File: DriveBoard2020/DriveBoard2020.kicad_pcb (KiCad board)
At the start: 2 copper layers, 78 parts, among them SW0 SW_SPST, SW1 SW_Push, SW2 SW_Push, SW3 SW_Push, SW4 SW_Push, SW5 SW_Push, SW6 SW_Push, SW7 SW_Push, SW8 SW_Push, SW9 SW_Push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

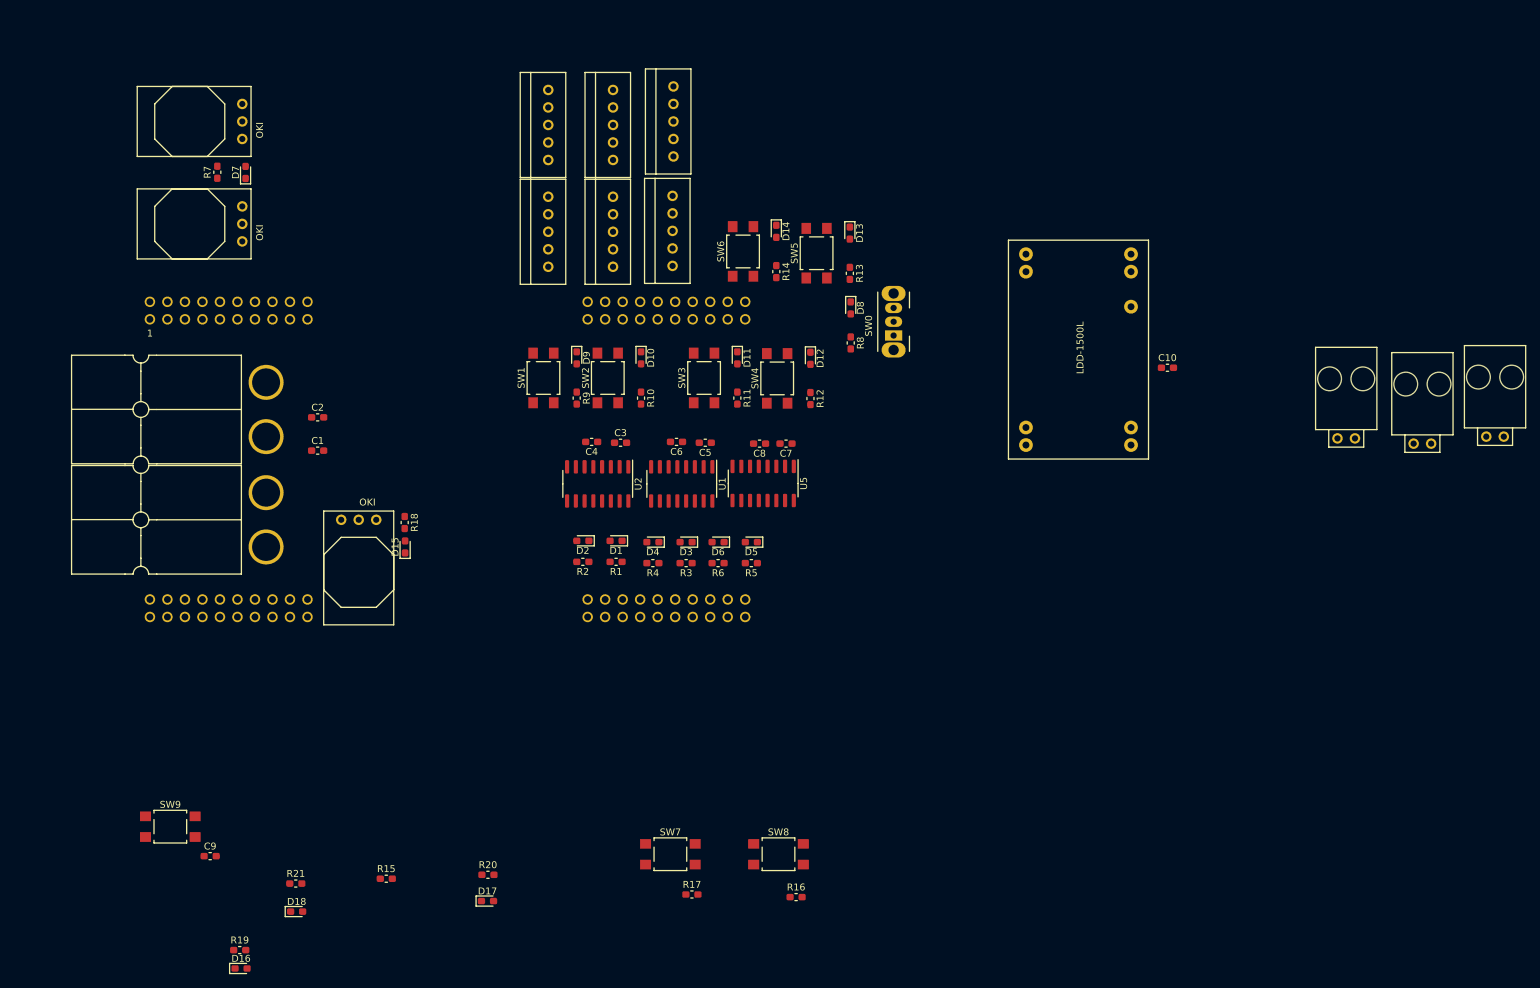
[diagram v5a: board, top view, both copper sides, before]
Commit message: finished placing components on layout
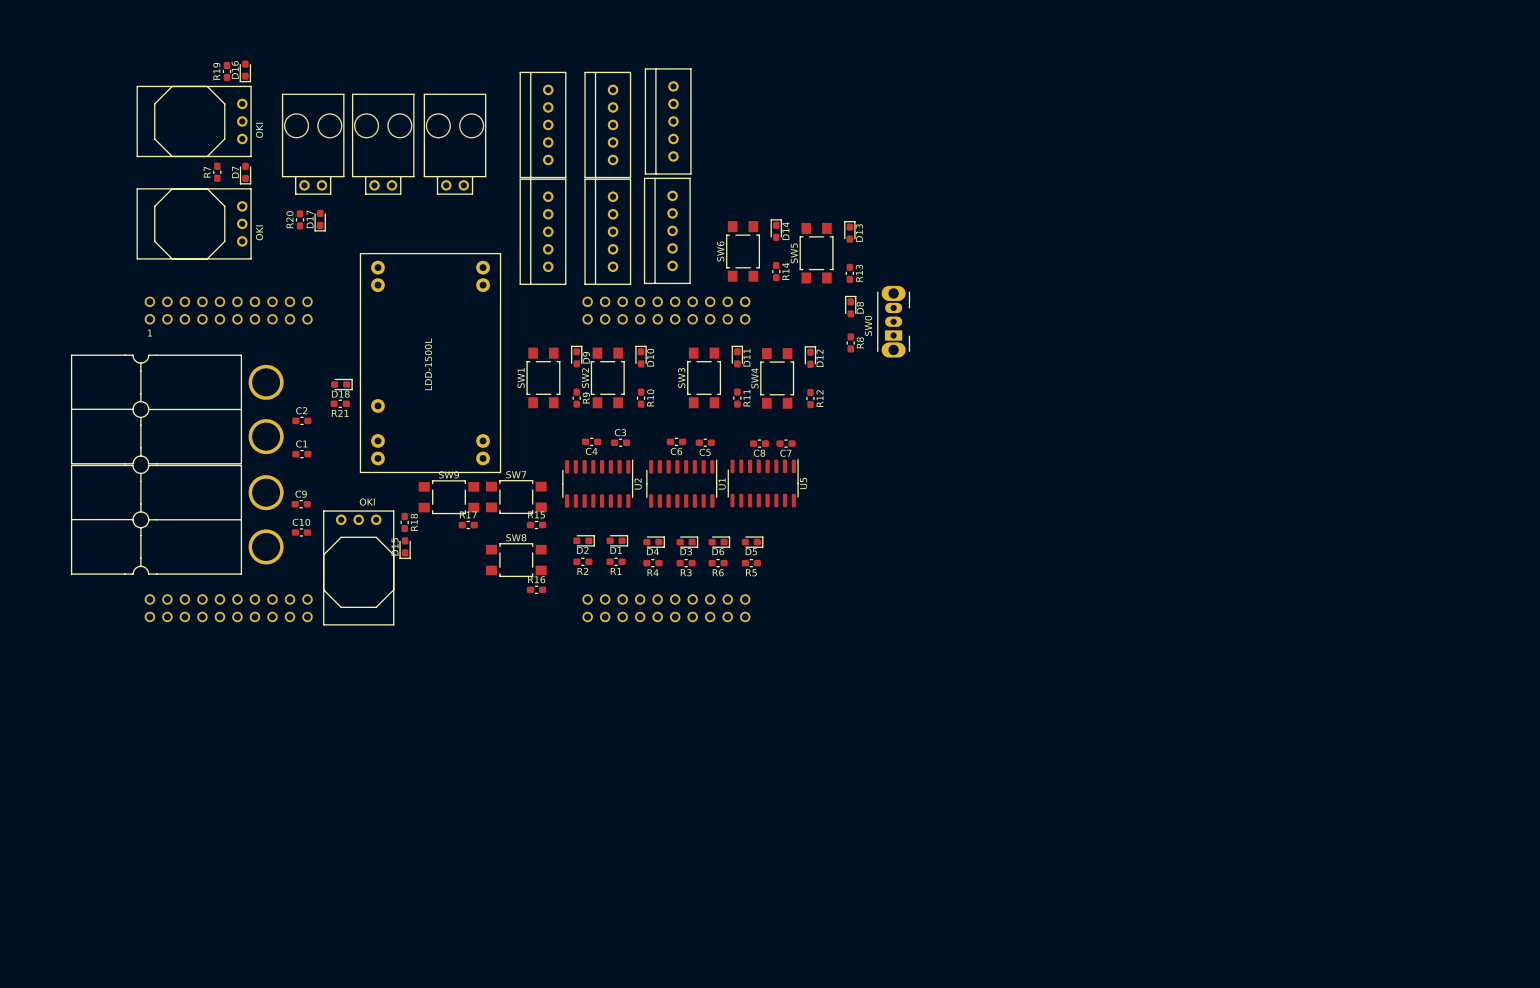
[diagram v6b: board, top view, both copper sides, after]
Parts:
- moved Conn11 155.3 mm to (108.2, 46.5)
- moved Conn10 155.2 mm to (118.6, 46.5)
- moved Conn9 154.3 mm to (98.0, 46.5)
- moved D16 130.3 mm to (88.2, 29.8), turned to 90 degrees
- moved C10 127.9 mm to (96.3, 96.8)
- moved R19 127.5 mm to (85.5, 30.0), turned to 90 degrees
- moved D17 101.8 mm to (99.1, 51.4), turned to 90 degrees
- moved R20 98.8 mm to (96.1, 51.5), turned to 90 degrees
- moved U8 79.5 mm to (125.2, 56.4), turned to 180 degrees
- moved D18 76.7 mm to (102.0, 75.4), turned to 180 degrees
- moved R21 69.9 mm to (102.0, 78.2), turned to 180 degrees
- moved R17 62.7 mm to (120.5, 95.8)
- moved SW9 62.6 mm to (117.7, 91.7)
- moved R16 58.4 mm to (130.4, 105.2)
- moved SW8 57.2 mm to (127.5, 100.8)
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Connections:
- Conn8 pad 2: (no net) -> +12VA
- U4 pad PA7: Headlight_OnOff_PWM -> Net-(U4-PadPA7)
- U4 pad PC7: Net-(U4-PadPC7) -> Headlight_OnOff_PWM
- U4 pad PF1: Dout_NeoPixel -> Net-(U4-PadPF1)
- U4 pad PP2: Net-(U4-PadPP2) -> Dout_NeoPixel

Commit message: traces to layout
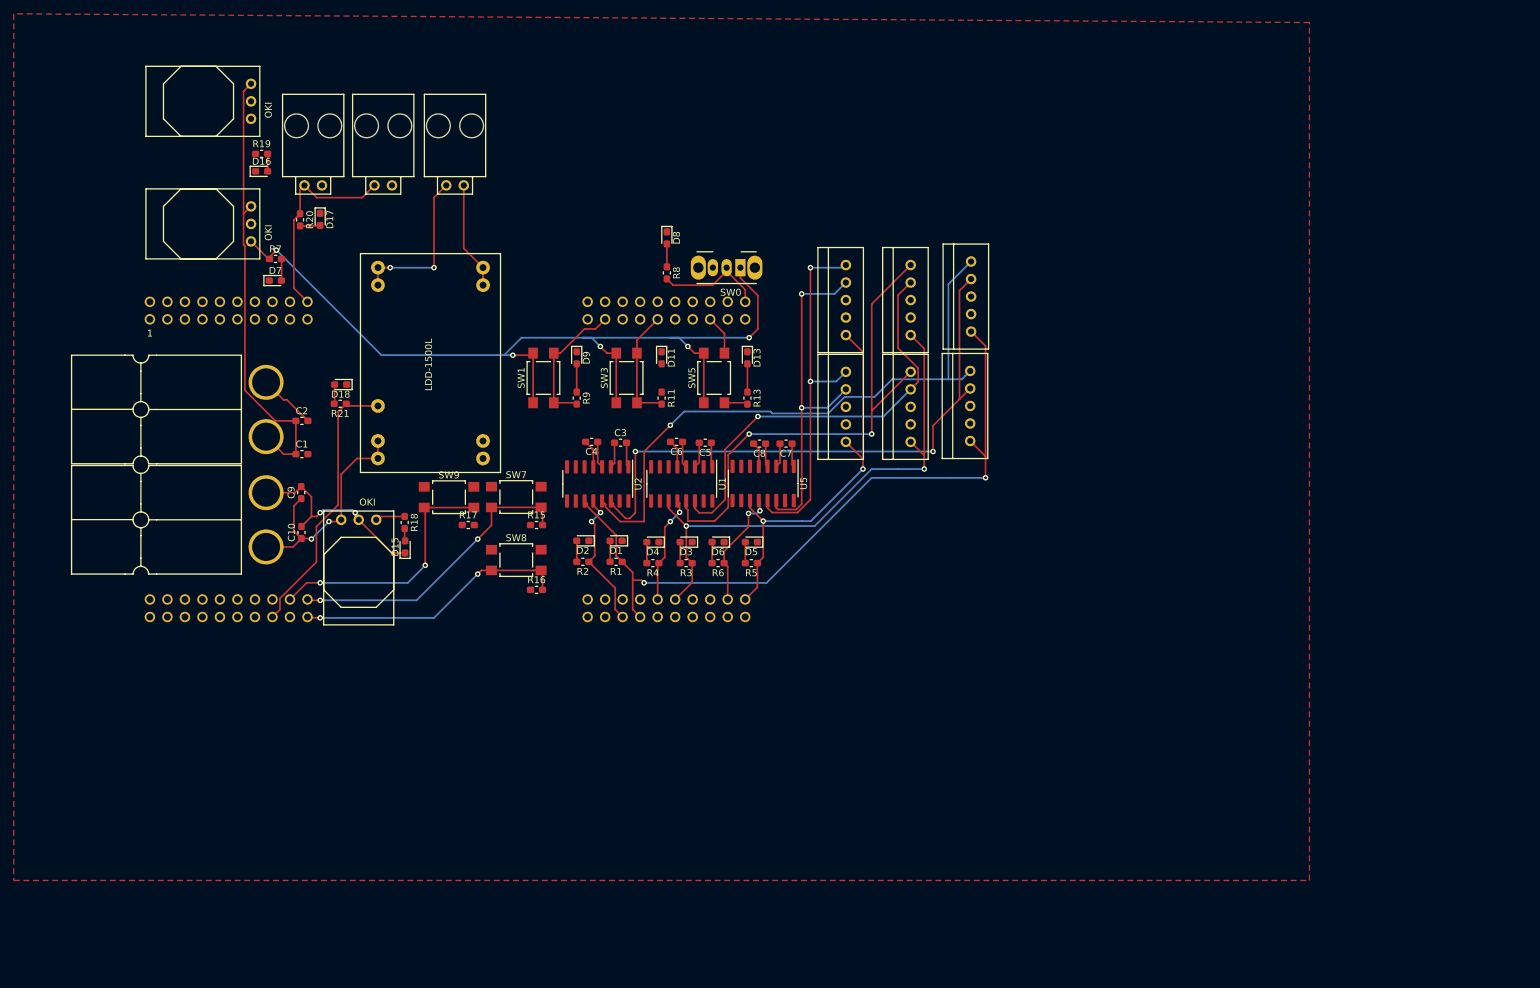
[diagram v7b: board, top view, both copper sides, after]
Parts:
- removed D10, D12, D14: LED, LED_SMD:LED_0603_1608Metric_Pad1.05x0.95mm_HandSolder
- removed R10, R12, R14: 500, Resistor_SMD:R_0603_1608Metric_Pad1.05x0.95mm_HandSolder
- removed SW2, SW4, SW6: SW_Push, Button_Switch_SMD:SW_SPST_TL3305A
- moved Conn2 50.1 mm to (193.5, 62.6)
- moved Conn4 50.1 mm to (175.3, 63.1)
- moved Conn7 50.1 mm to (175.3, 78.6)
- moved Conn3 50.1 mm to (184.7, 63.1)
- moved Conn5 50.1 mm to (193.4, 78.5)
- moved Conn6 50.1 mm to (184.7, 78.6)
- moved D8 28.5 mm to (149.4, 54.1)
- moved R8 28.5 mm to (149.4, 59.2)
- moved SW0 24.3 mm to (160.0, 58.4), turned to 180 degrees
- moved D13 23.4 mm to (161.0, 71.5)
- moved R13 23.4 mm to (161.0, 77.3)
- moved SW5 23.4 mm to (156.2, 74.4)
- moved D7 16.3 mm to (92.6, 60.3), turned to 0 degrees
- moved R7 15.1 mm to (92.6, 57.1), turned to 0 degrees
- moved D16 14.9 mm to (90.6, 44.5), turned to 0 degrees
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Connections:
- R11 pad 2: ML_Motor -> Middle_Motor
- R13 pad 2: RL_Motor -> Rear_Motor
- R19 pad 1: +5VL -> +5V
- R9 pad 2: FL_Motor -> Front_Motor
- SW1 pad 2: FL_Motor -> Front_Motor
- SW3 pad 2: ML_Motor -> Middle_Motor
- SW5 pad 2: RL_Motor -> Rear_Motor
- U4 pad PB3: Net-(U4-PadPB3) -> NeoPixel_White
- U4 pad PH1: ML_Motor -> Rear_Motor
- U4 pad PK4: Net-(U4-PadPK4) -> Front_Motor
- U4 pad PK5: FL_Motor -> Net-(U4-PadPK5)
- U4 pad PK6: MR_Motor -> Net-(U4-PadPK6)
- U4 pad PL4: NeoPixel_White -> Net-(U4-PadPL4)
- U4 pad PL5: NeoPixel_Pattern -> Net-(U4-PadPL5)
- U4 pad PM0: FR_Motor -> Net-(U4-PadPM0)
- U4 pad PM1: Net-(U4-PadPM1) -> Middle_Motor
- U4 pad PM3: Headlight_Power -> Net-(U4-PadPM3)
- U4 pad PM4: Net-(U4-PadPM4) -> NeoPixel_Pattern
- U4 pad PM5: Net-(U4-PadPM5) -> Headlight_Power
- U4 pad PP3: RR_Motor -> Net-(U4-PadPP3)
- U4 pad PQ1: RL_Motor -> Net-(U4-PadPQ1)
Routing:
- net +3V3: track 0.00 -> 130.6 mm, vias 0 -> 5
- net Tx6: track 0.00 -> 103.0 mm, vias 0 -> 2
- net R1_In: track 0.00 -> 88.5 mm, vias 0 -> 1
- net T1_Out: track 0.00 -> 86.7 mm, vias 0 -> 2
- net Tx4: track 0.00 -> 77.7 mm, vias 0 -> 2
- net R2_In: track 0.00 -> 74.2 mm, vias 0 -> 2
- net +12V: track 0.00 -> 66.0 mm
- net T2_Out: track 0.00 -> 62.3 mm, vias 0 -> 1
- net Tx3: track 0.00 -> 57.8 mm, vias 0 -> 2
- net R3_In: track 0.00 -> 53.0 mm, vias 0 -> 3
- net T3_Out: track 0.00 -> 50.3 mm, vias 0 -> 2
- net Headlight_Power: track 0.00 -> 43.7 mm, vias 0 -> 2
- net Headlight_OnOff_PWM: track 0.00 -> 40.1 mm
- net NeoPixel_White: track 0.00 -> 39.7 mm, vias 0 -> 2
- net NeoPixel_Pattern: track 0.00 -> 37.3 mm, vias 0 -> 2
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- added copper zone on F.Cu, net GND

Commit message: edge cuts
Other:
- board outline added: 124.5 x 107.4 mm
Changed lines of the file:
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@@
   (general
     (thickness 1.6)
-    (drawings 0)
+    (drawings 20)
     (tracks 394)
     (zones 0)
@@
     )
   )
+  (gr_line (start 73.152 28.321) (end 197.612 28.321) (layer Edge.Cuts) (width 0.05))
+  (gr_line (start 73.152 54.483) (end 73.152 28.321) (layer Edge.Cuts) (width 0.05))
+  (gr_line (start 73.152 121.031) (end 73.152 54.483) (layer Edge.Cuts) (width 0.05))
+  (gr_arc (start 73.152 123.063) (end 73.152 125.095) (angle -180) (layer Edge.Cuts) (width 0.05))
+  (gr_line (start 73.152 133.731) (end 73.152 125.095) (layer Edge.Cuts) (width 0.05))
+  (gr_arc (start 75.184 133.731) (end 73.152 133.731) (angle -90) (layer Edge.Cuts) (width 0.05))
+  (gr_line (start 124.587 135.763) (end 75.184 135.763) (layer Edge.Cuts) (width 0.05))
+  (gr_line (start 197.612 54.483) (end 197.612 28.321) (layer Edge.Cuts) (width 0.05))
+  (gr_line (start 197.612 88.011) (end 197.612 54.483) (layer Edge.Cuts) (width 0.05))
+  (gr_arc (start 195.58 88.011) (end 195.58 90.043) (angle -90) (layer Edge.Cuts) (width 0.05))
+  (gr_line (start 195.453 90.043) (end 195.58 90.043) (layer Edge.Cuts) (width 0.05))
+  (gr_line (start 179.705 90.043) (end 195.453 90.043) (layer Edge.Cuts) (width 0.05))
+  (gr_line (start 179.705 110.871) (end 179.705 90.043) (layer Edge.Cuts) (width 0.05))
+  (gr_line (start 195.58 110.871) (end 179.705 110.871) (layer Edge.Cuts) (width 0.05))
+  (gr_arc (start 195.58 112.903) (end 197.612 112.903) (angle -90) (layer Edge.Cuts) (width 0.05))
+  (gr_line (start 197.612 121.031) (end 197.612 112.903) (layer Edge.Cuts) (width 0.05))
+  (gr_arc (start 197.612 123.063) (end 197.612 121.031) (angle -180) (layer Edge.Cuts) (width 0.05))
+  (gr_line (start 197.612 133.731) (end 197.612 125.095) (layer Edge.Cuts) (width 0.05))
+  (gr_arc (start 195.58 133.731) (end 195.58 135.763) (angle -90) (layer Edge.Cuts) (width 0.05))
+  (gr_line (start 124.587 135.763) (end 195.58 135.763) (layer Edge.Cuts) (width 0.05))
   (segment (start 96.782928 80.145928) (end 97.282 80.645) (width 0.25) (layer F.Cu) (net 1))
   (segment (start 94.233999 77.596999) (end 96.782928 80.145928) (width 0.25) (layer F.Cu) (net 1))
@@
   (segment (start 191.80175 77.50175) (end 193.3575 75.946) (width 0.25) (layer F.Cu) (net 44))
   (segment (start 187.96 81.3435) (end 191.80175 77.50175) (width 0.25) (layer F.Cu) (net 44))
-  (segment (start 132.945 71.872) (end 132.945 78.022) (width 0.25) (layer F.Cu) (net 133))
-  (segment (start 132.945 70.822) (end 132.945 71.872) (width 0.25) (layer F.Cu) (net 133))
-  (segment (start 136.075 78.022) (end 136.271 78.218) (width 0.25) (layer F.Cu) (net 133))
-  (segment (start 132.945 78.022) (end 136.075 78.022) (width 0.25) (layer F.Cu) (net 133))
-  (segment (start 133.895 70.822) (end 137.407 67.31) (width 0.25) (layer F.Cu) (net 133))
-  (segment (start 132.945 70.822) (end 133.895 70.822) (width 0.25) (layer F.Cu) (net 133))
   (segment (start 95.844428 97.213428) (end 96.3435 97.7125) (width 0.25) (layer F.Cu) (net 69))
   (segment (start 95.25 96.619) (end 95.844428 97.213428) (width 0.25) (layer F.Cu) (net 69))
@@
   (segment (start 101.65799 92.849008) (end 98.515001 95.991997) (width 0.25) (layer F.Cu) (net 83))
   (segment (start 102.842 78.1685) (end 101.65799 79.35251) (width 0.25) (layer F.Cu) (net 83))
+  (segment (start 132.945 71.872) (end 132.945 78.022) (width 0.25) (layer F.Cu) (net 133))
+  (segment (start 132.945 70.822) (end 132.945 71.872) (width 0.25) (layer F.Cu) (net 133))
+  (segment (start 136.075 78.022) (end 136.271 78.218) (width 0.25) (layer F.Cu) (net 133))
+  (segment (start 132.945 78.022) (end 136.075 78.022) (width 0.25) (layer F.Cu) (net 133))
+  (segment (start 133.895 70.822) (end 137.407 67.31) (width 0.25) (layer F.Cu) (net 133))
+  (segment (start 132.945 70.822) (end 133.895 70.822) (width 0.25) (layer F.Cu) (net 133))
   (segment (start 139.0015 67.31) (end 137.407 67.31) (width 0.25) (layer F.Cu) (net 133))
   (segment (start 140.3985 65.913) (end 139.0015 67.31) (width 0.25) (layer F.Cu) (net 133))
